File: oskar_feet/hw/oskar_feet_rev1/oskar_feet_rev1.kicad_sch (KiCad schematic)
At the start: 11 parts, among them J1 Conn_02x04_Odd_Even, U1 ATmega2560-16A, Y1 16MHz

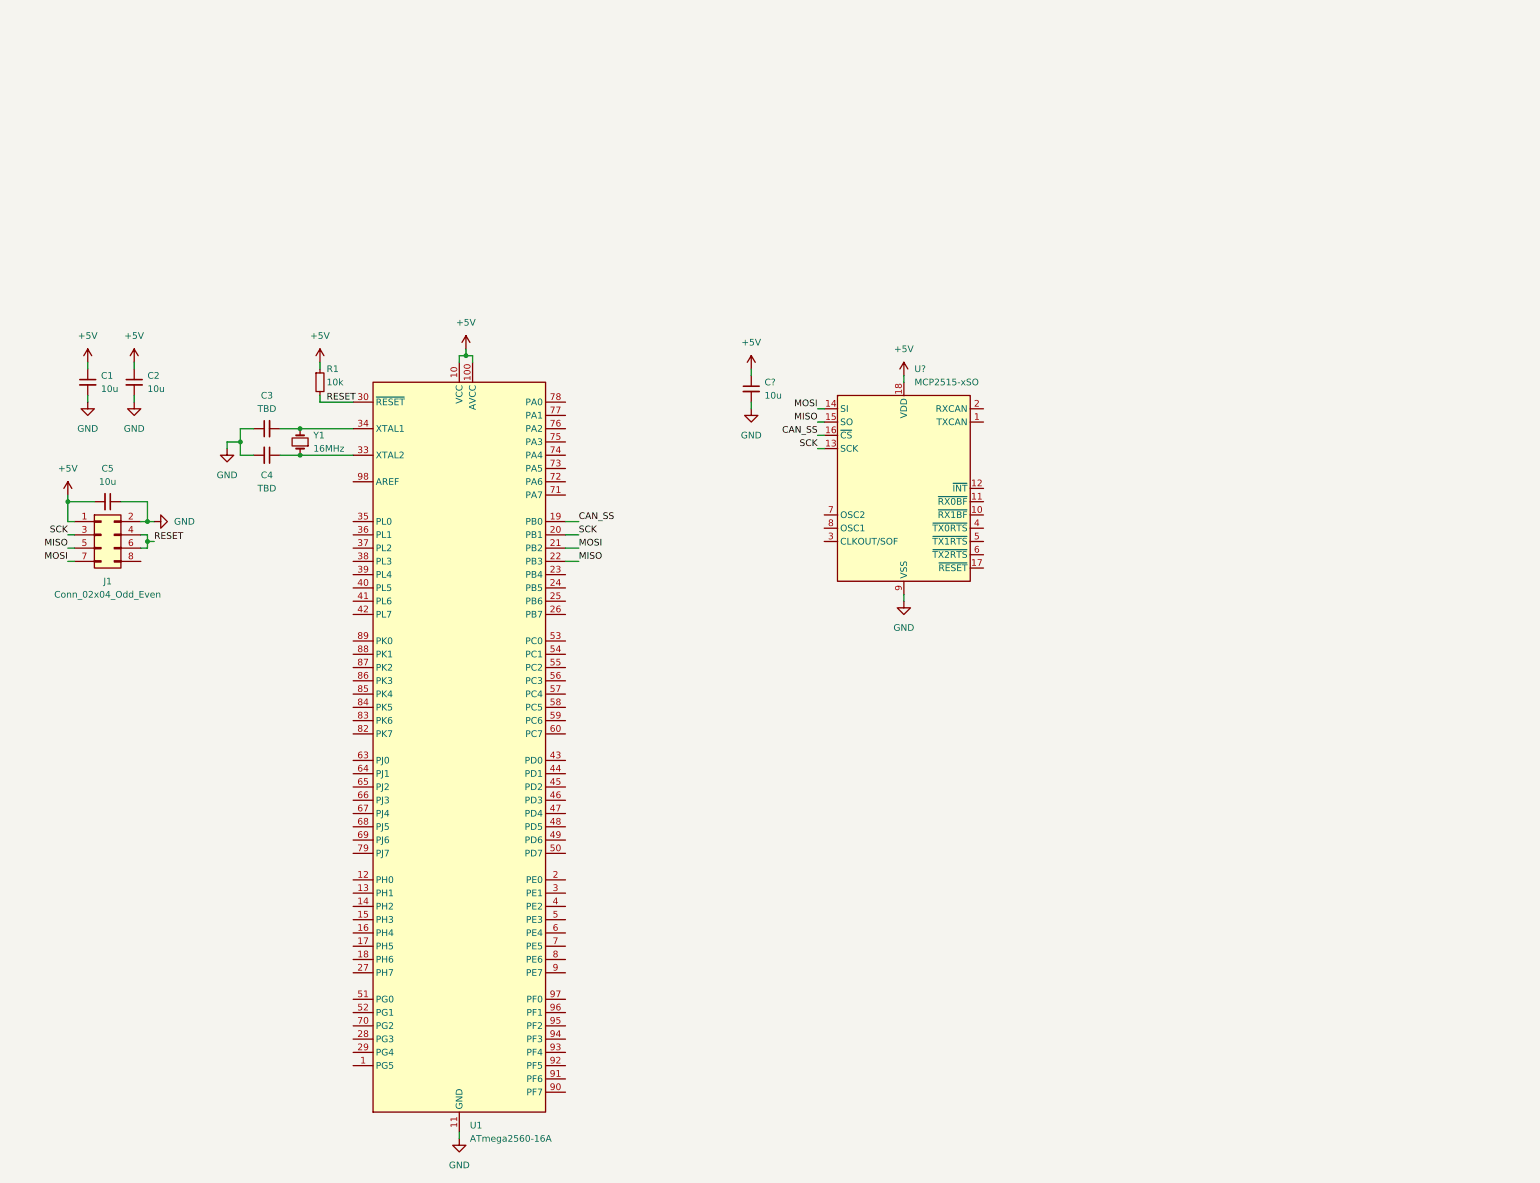
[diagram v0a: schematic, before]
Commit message: Feet controller. Start some bits of layouting. Add Motor power relay
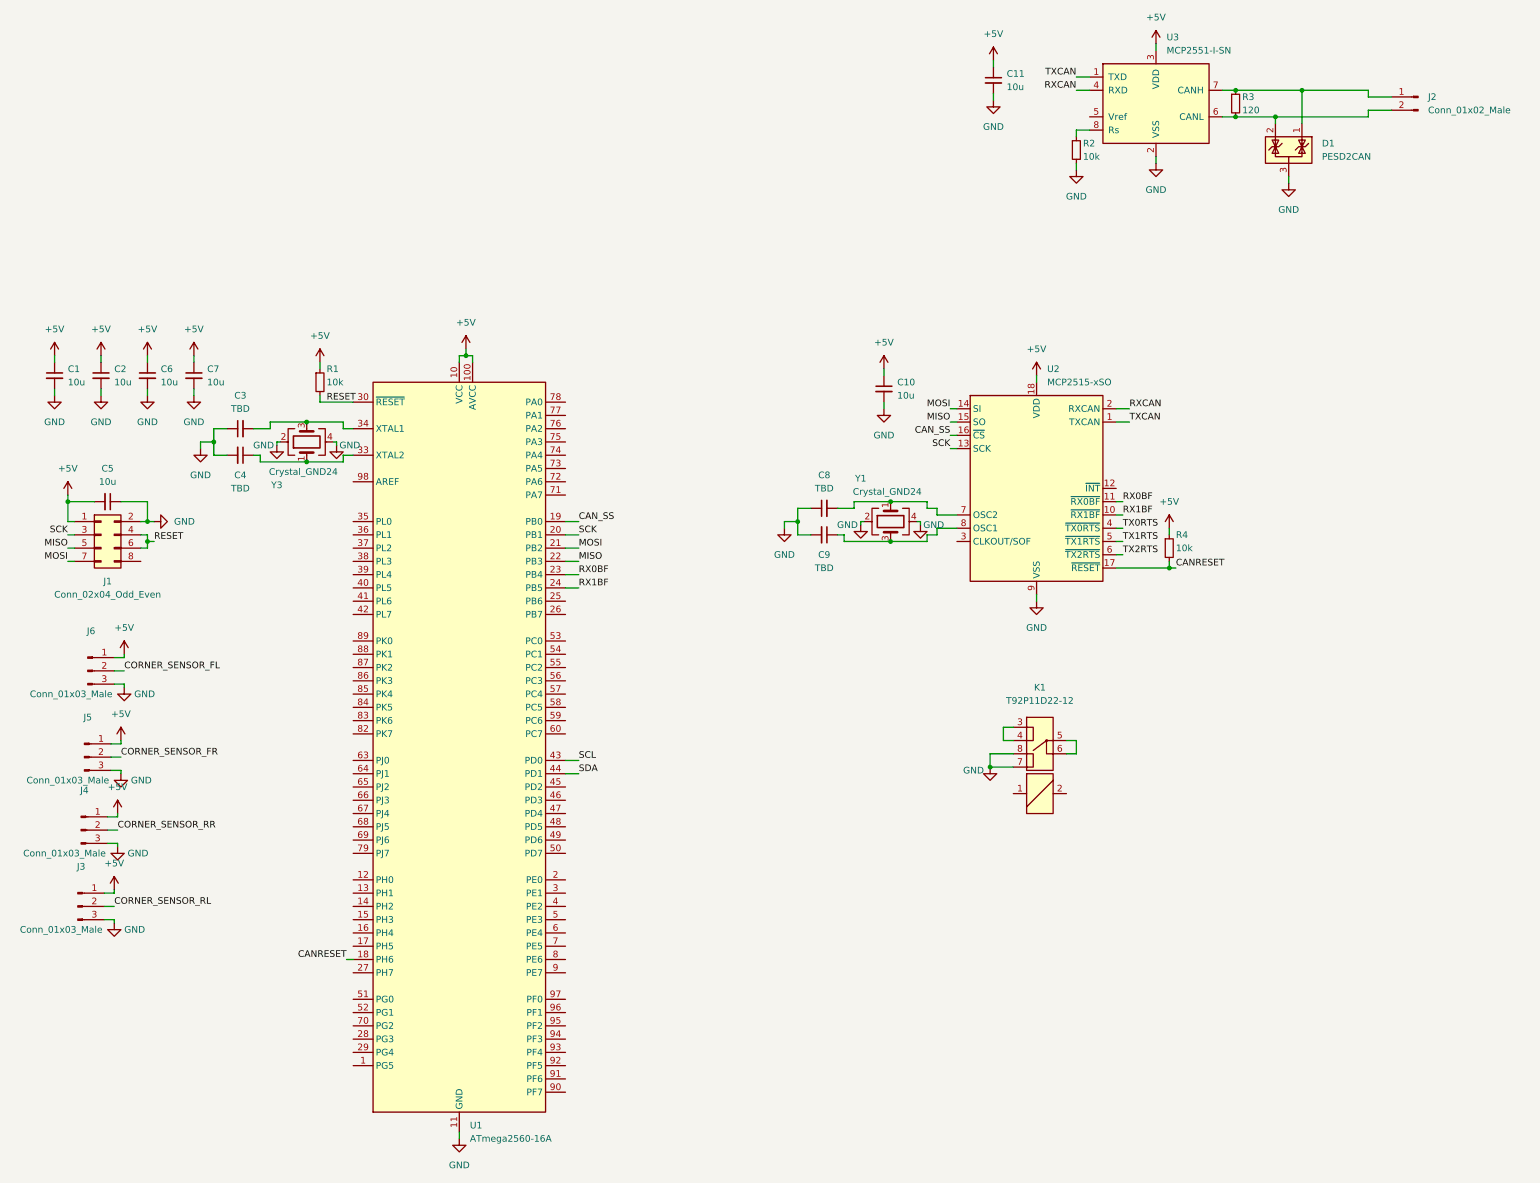
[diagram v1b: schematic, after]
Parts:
- removed Y1: 16MHz, symbol Device:Crystal_Small
- added C11, C6, C7: 10u, Capacitor_SMD:C_0603_1608Metric, symbol Device:C_Small
- added C8, C9: TBD, Capacitor_SMD:C_0603_1608Metric, symbol Device:C_Small
- added D1: PESD2CAN, Package_TO_SOT_SMD:SOT-23, symbol Power_Protection:NUP2105L
- added J2: Conn_01x02_Male, Connector_Molex:Molex_KK-254_AE-6410-02A_1x02_P2.54mm_Vertical, symbol Connector:Conn_01x02_Male
- added J3, J4, J5, J6: Conn_01x03_Male, Connector_Molex:Molex_KK-254_AE-6410-03A_1x03_P2.54mm_Vertical, symbol Connector:Conn_01x03_Male
- added K1: T92P11D22-12, Oskar:T92P11D22-12, symbol Oskar:T92P11D22-12
- added R2, R4: 10k, Resistor_SMD:R_0603_1608Metric, symbol Device:R_Small
- added R3: 120, Resistor_SMD:R_0603_1608Metric, symbol Device:R_Small
- added U3: MCP2551-I-SN, Package_SO:SOIC-8_3.9x4.9mm_P1.27mm, symbol Interface_CAN_LIN:MCP2551-I-SN
- added Y1, Y3: Crystal_GND24, Crystal:Crystal_SMD_Abracon_ABM8G-4Pin_3.2x2.5mm, symbol Device:Crystal_GND24
- gave numbers to parts that had none: 2
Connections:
- net +5V: now also C11.1, C6.1, C7.1, J3.1 (Pin_1), J4.1 (Pin_1), J5.1 (Pin_1), J6.1 (Pin_1), R4.1, U3.3 (VDD)
- net GND: now also C11.2, C6.2, C7.2, C8.1, C9.2, D1.3 (A), J3.3 (Pin_3), J4.3 (Pin_3), J5.3 (Pin_3), J6.3 (Pin_3), K1.7, K1.8, R2.2, U3.2 (VSS), Y1.2, Y1.4, Y3.2, Y3.4
- net at C4.1, U1.33 (XTAL2): now also Y3.1
- net at C3.2, U1.34 (XTAL1): now also Y3.3
- net TXCAN: now reaches U2.1 (TXCAN)
- net TXCAN: now also U3.1 (TXD)
- net RX1BF: now reaches U2.10 (~{RX1BF})
- net RX1BF: now also U1.24 (PB5)
- net RX0BF: now reaches U2.11 (~{RX0BF})
- net RX0BF: now also U1.23 (PB4)
- net CANRESET: now reaches U2.17 (~{RESET})
- net CANRESET: now also U1.18 (PH6), R4.2
- net RXCAN: now reaches U2.2 (RXCAN)
- net RXCAN: now also U3.4 (RXD)
- net TX0RTS: now reaches U2.4 (~{TX0RTS})
- net TX1RTS: now reaches U2.5 (~{TX1RTS})
- net TX2RTS: now reaches U2.6 (~{TX2RTS})
- net at U2.7 (OSC2): now also C8.2, Y1.1
- net at U2.8 (OSC1): now also C9.1, Y1.3
- net SCL: now reaches U1.43 (PD0)
- net SDA: now reaches U1.44 (PD1)
- new net: D1.1 (K), J2.1 (Pin_1), R3.1, U3.7 (CANH)
- new net: D1.2 (K), J2.2 (Pin_2), R3.2, U3.6 (CANL)
- new net: R2.1, U3.8 (Rs)
- new net: K1.3, K1.4
- new net: K1.5, K1.6
- new net CORNER_SENSOR_FL: J6.2 (Pin_2)
- new net CORNER_SENSOR_FR: J5.2 (Pin_2)
- new net CORNER_SENSOR_RL: J3.2 (Pin_2)
- new net CORNER_SENSOR_RR: J4.2 (Pin_2)
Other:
- moved on the sheet: C1, C10, C2, C3, C4, U2
